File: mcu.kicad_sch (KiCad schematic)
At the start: 23 parts, among them IC3 STM32G473RCT6, J1 USB4105-GF-A-120, Y1 ECS-240-6-37B-7KM-TR

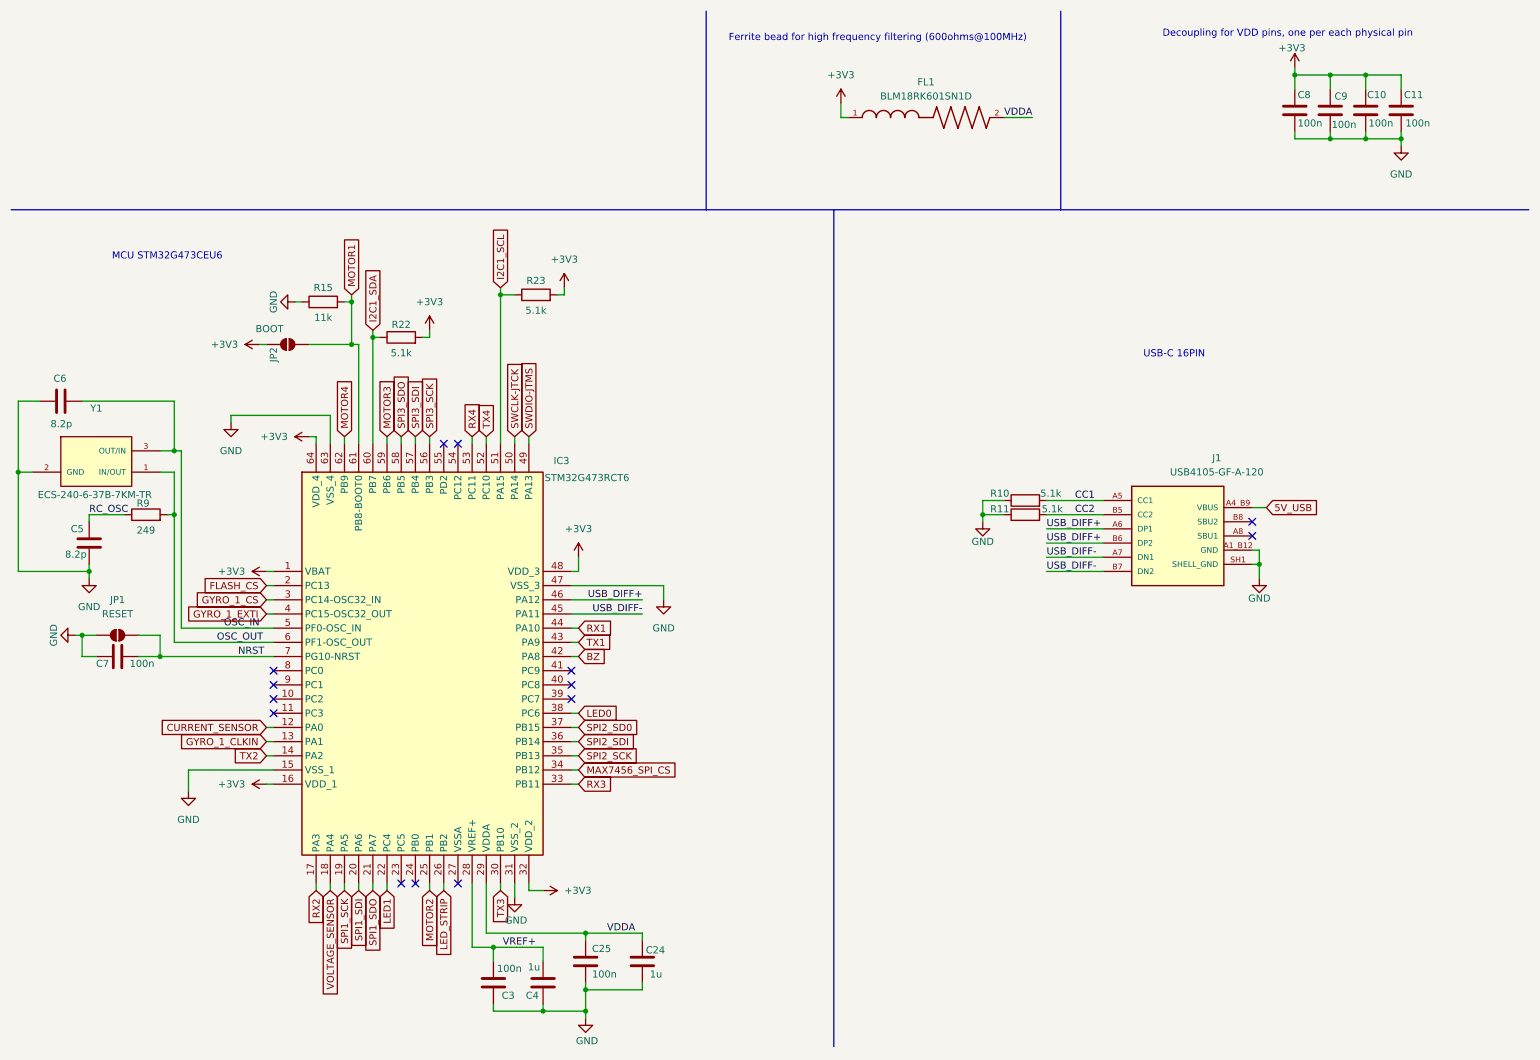
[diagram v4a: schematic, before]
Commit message: add microsd card connector
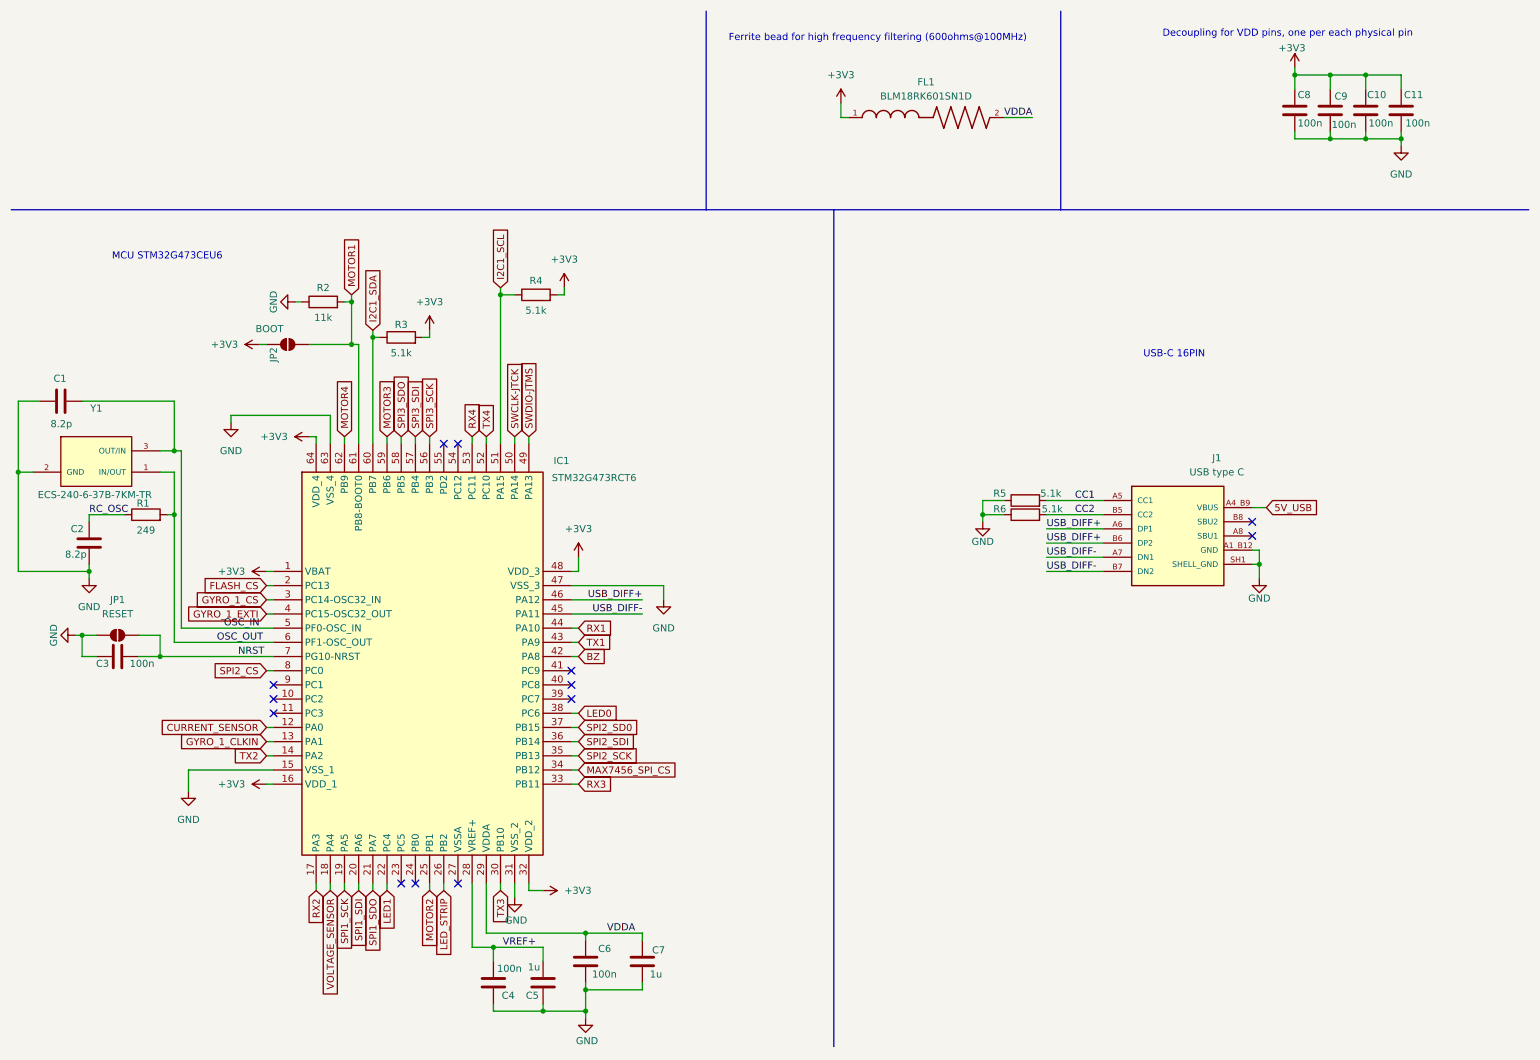
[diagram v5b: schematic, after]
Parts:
- J1: value USB4105-GF-A-120 -> USB type C; LCSC Part Name C5184243 -> C2765186; Manufacturer_Name Global Connector Technology -> Global SHOU HAN; Manufacturer_Part_Number USB4105-GF-A-120 -> TYPE-C 16PIN 2MD(073)
- renumbered C6 to C1, C5 to C2, C7 to C3, C3 to C4, C4 to C5, C25 to C6, C24 to C7, IC3 to IC1, R9 to R1, R15 to R2, R22 to R3, R23 to R4, R10 to R5, R11 to R6
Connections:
- net SPI2_CS: now reaches IC1.8 (PC0)
- no-connect marks 14 -> 13
